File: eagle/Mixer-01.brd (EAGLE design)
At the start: 95 x 72 mm, 58 parts, among them IC1 TL072P, IC2 TL072P, IC3 LM4558N

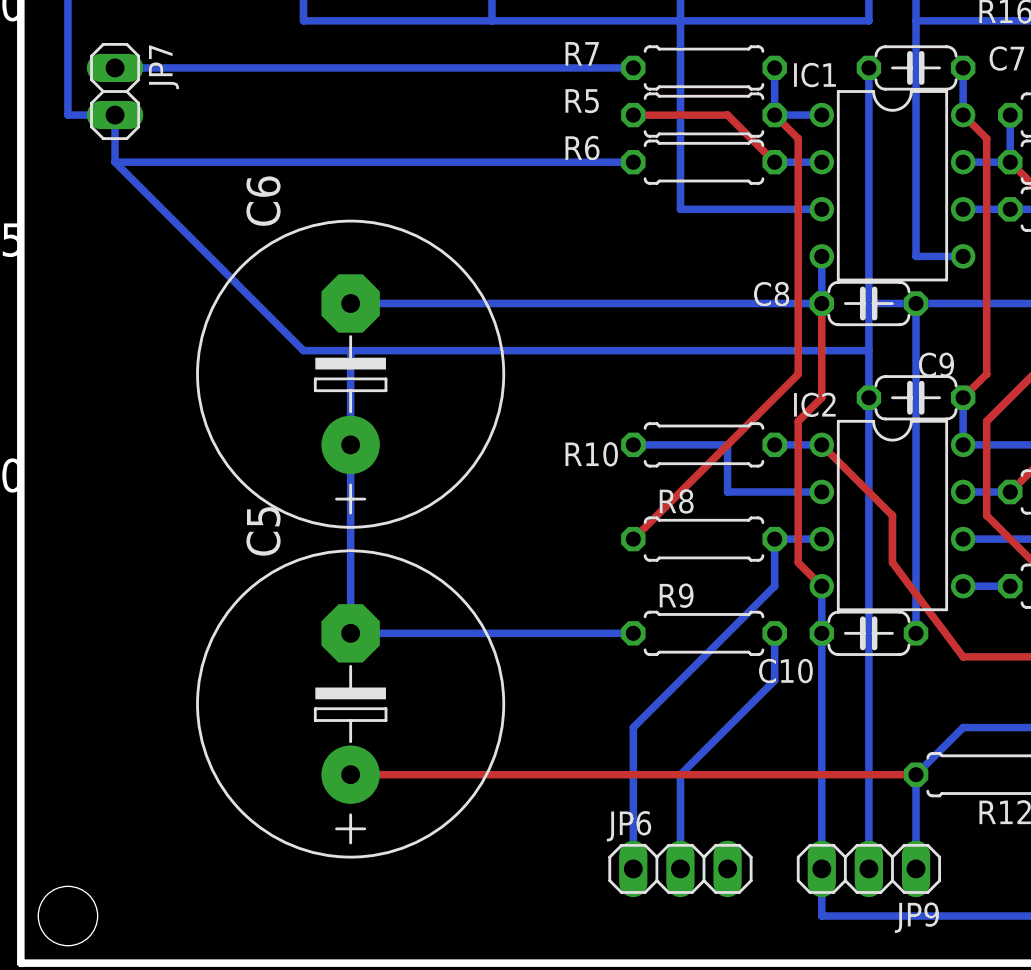
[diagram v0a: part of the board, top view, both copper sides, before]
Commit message: Mixer-01.brd: 修正
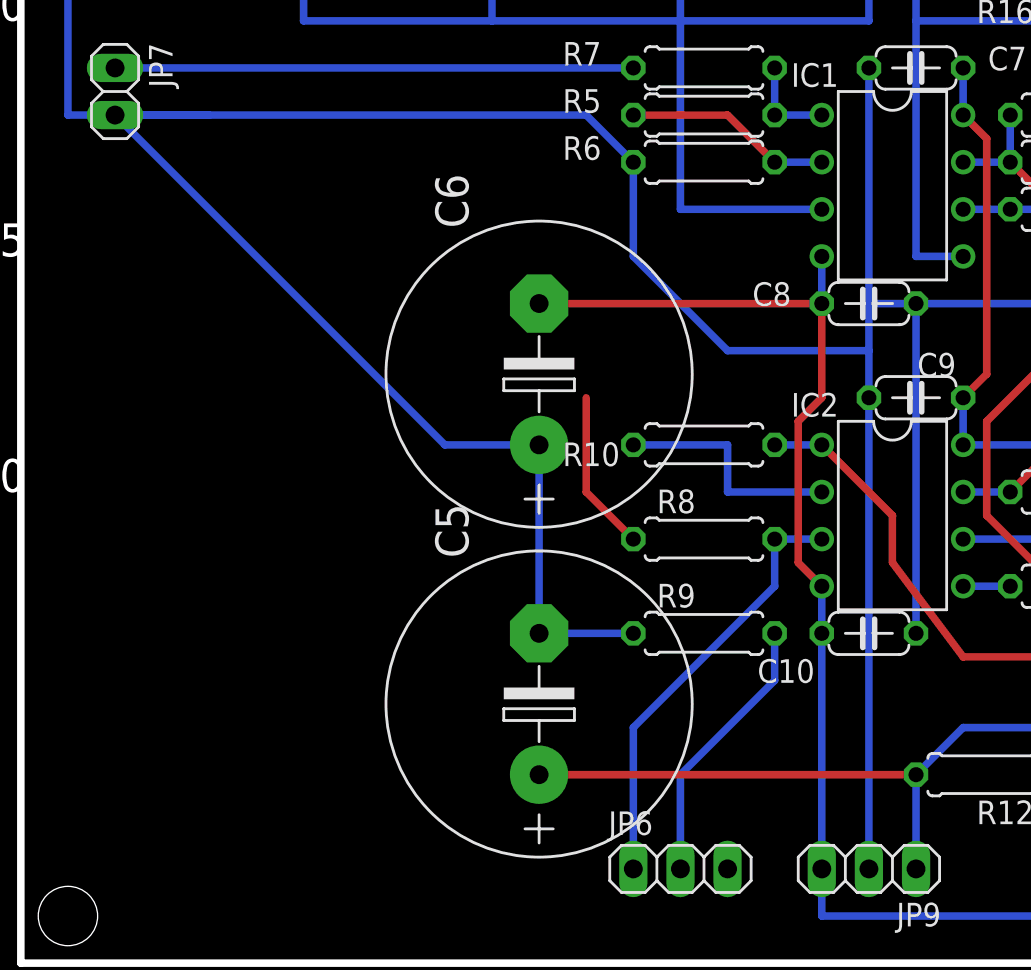
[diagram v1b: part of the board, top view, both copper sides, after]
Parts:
- C5, C6: device resistor:E7,5-16 -> rcl:E7,5-16
- moved C5 10.2 mm to (27.9, 14.0)
- moved C6 10.2 mm to (27.9, 31.8)
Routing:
- net N$15: track 32.1 -> 13.8 mm
- net V-: track 114.9 -> 104.8 mm
- net V+: track 99.2 -> 89.1 mm
- net GND: track 269.4 -> 263.0 mm
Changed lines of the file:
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@@
 <layer number="97" name="Info" color="7" fill="1" visible="no" active="no"/>
 <layer number="98" name="Guide" color="6" fill="1" visible="no" active="no"/>
-<layer number="100" name="Grid" color="7" fill="1" visible="yes" active="yes"/>
+<layer number="100" name="Grid" color="7" fill="1" visible="no" active="yes"/>
 <layer number="101" name="Jumper" color="14" fill="1" visible="yes" active="yes"/>
+<layer number="102" name="outline" color="15" fill="1" visible="yes" active="yes"/>
 </layers>
 <board>
@@
 <wire x1="38.1" y1="5.08" x2="38.1" y2="25.4" width="0.4064" layer="101"/>
 <wire x1="0" y1="12.7" x2="93.98" y2="12.7" width="0.254" layer="100"/>
+<wire x1="27.94" y1="39.37" x2="2.54" y2="39.37" width="0.0254" layer="102"/>
+<wire x1="2.54" y1="39.37" x2="2.54" y2="24.13" width="0.0254" layer="102"/>
+<wire x1="2.54" y1="24.13" x2="27.94" y2="24.13" width="0.0254" layer="102"/>
+<wire x1="27.94" y1="24.13" x2="27.94" y2="39.37" width="0.0254" layer="102"/>
+<wire x1="27.94" y1="21.59" x2="2.54" y2="21.59" width="0.0254" layer="102"/>
+<wire x1="2.54" y1="21.59" x2="2.54" y2="6.35" width="0.0254" layer="102"/>
+<wire x1="2.54" y1="6.35" x2="27.94" y2="6.35" width="0.0254" layer="102"/>
+<wire x1="27.94" y1="6.35" x2="27.94" y2="21.59" width="0.0254" layer="102"/>
+<wire x1="30.48" y1="30.48" x2="40.64" y2="45.72" width="0.4064" layer="101"/>
 </plain>
 <attributes>
@@
 <element name="JP10" library="pinhead" package="1X02" value="LED" x="57.15" y="5.08"/>
 <element name="R12" library="resistor" package="0207/7" value="1k" x="52.07" y="10.16" rot="R180"/>
-<element name="C5" library="resistor" package="E7,5-16" value="470u" x="17.78" y="13.97" rot="R90"/>
-<element name="C6" library="resistor" package="E7,5-16" value="470u" x="17.78" y="31.75" rot="R90"/>
+<element name="C5" library="rcl" package="E7,5-16" value="470u" x="27.94" y="13.97" rot="R90"/>
+<element name="C6" library="rcl" package="E7,5-16" value="470u" x="27.94" y="31.75" rot="R90"/>
 <element name="C7" library="resistor" package="C050-024X044" value="0.1u" x="48.26" y="48.26" smashed="yes" rot="R180">
 <attribute name="NAME" x="54.229" y="49.403" size="1.27" layer="25" ratio="10" rot="R180"/>
@@
 <wire x1="55.88" y1="12.7" x2="50.8" y2="12.7" width="0.4064" layer="16"/>
 <wire x1="50.8" y1="12.7" x2="48.26" y2="10.16" width="0.4064" layer="16"/>
-<wire x1="17.78" y1="10.16" x2="48.26" y2="10.16" width="0.4064" layer="1"/>
+<wire x1="27.94" y1="10.16" x2="48.26" y2="10.16" width="0.4064" layer="1"/>
 <wire x1="50.8" y1="45.72" x2="52.07" y2="44.45" width="0.4064" layer="1"/>
 <wire x1="52.07" y1="44.45" x2="52.07" y2="31.75" width="0.4064" layer="1"/>
 <wire x1="52.07" y1="31.75" x2="50.8" y2="30.48" width="0.4064" layer="1"/>
-<wire x1="68.58" y1="27.94" x2="63.5" y2="27.94" width="0" layer="19" extent="16-16"/>
 <wire x1="48.26" y1="5.08" x2="48.26" y2="10.16" width="0.4064" layer="16"/>
+<wire x1="63.5" y1="27.94" x2="68.58" y2="27.94" width="0" layer="19" extent="16-16"/>
 </signal>
 <signal name="V-">
@@
 <wire x1="58.42" y1="2.54" x2="58.42" y2="5.08" width="0.4064" layer="16"/>
 <wire x1="43.18" y1="35.56" x2="43.18" y2="38.1" width="0.4064" layer="16"/>
-<wire x1="17.78" y1="35.56" x2="43.18" y2="35.56" width="0.4064" layer="16"/>
 <wire x1="81.28" y1="20.32" x2="78.74" y2="20.32" width="0.4064" layer="16"/>
 <wire x1="78.74" y1="20.32" x2="78.74" y2="15.24" width="0.4064" layer="16"/>
@@
 <wire x1="41.91" y1="29.21" x2="41.91" y2="21.59" width="0.4064" layer="1"/>
 <wire x1="41.91" y1="21.59" x2="43.18" y2="20.32" width="0.4064" layer="1"/>
+<wire x1="27.94" y1="35.56" x2="43.18" y2="35.56" width="0.4064" layer="1"/>
 </signal>
 <signal name="GND">
@@
 <contactref element="R21" pad="1"/>
 <wire x1="45.72" y1="48.26" x2="45.72" y2="35.56" width="0.4064" layer="16"/>
-<wire x1="45.72" y1="35.56" x2="45.72" y2="33.02" width="0.4064" layer="16"/>
 <wire x1="48.26" y1="35.56" x2="48.26" y2="17.78" width="0.4064" layer="16"/>
 <wire x1="45.72" y1="5.08" x2="45.72" y2="30.48" width="0.4064" layer="16"/>
@@
 <wire x1="60.96" y1="35.56" x2="48.26" y2="35.56" width="0.4064" layer="16"/>
 <wire x1="60.96" y1="40.64" x2="60.96" y2="35.56" width="0.4064" layer="16"/>
-<wire x1="17.78" y1="17.78" x2="17.78" y2="27.94" width="0.4064" layer="16"/>
-<wire x1="17.78" y1="17.78" x2="33.02" y2="17.78" width="0.4064" layer="16"/>
+<wire x1="27.94" y1="17.78" x2="27.94" y2="27.94" width="0.4064" layer="16"/>
+<wire x1="27.94" y1="17.78" x2="33.02" y2="17.78" width="0.4064" layer="16"/>
 <wire x1="45.72" y1="30.48" x2="45.72" y2="33.02" width="0.4064" layer="16"/>
-<wire x1="45.72" y1="33.02" x2="17.78" y2="33.02" width="0.4064" layer="16"/>
-<wire x1="17.78" y1="33.02" x2="17.78" y2="27.94" width="0.4064" layer="16"/>
-<wire x1="17.78" y1="33.02" x2="15.24" y2="33.02" width="0.4064" layer="16"/>
-<wire x1="5.08" y1="43.18" x2="5.08" y2="45.72" width="0.4064" layer="16"/>
+<wire x1="45.72" y1="33.02" x2="45.72" y2="35.56" width="0.4064" layer="16"/>
 <wire x1="88.9" y1="25.4" x2="91.44" y2="25.4" width="0.4064" layer="16"/>
 <wire x1="91.44" y1="25.4" x2="91.44" y2="43.18" width="0.4064" layer="16"/>
 <wire x1="91.44" y1="43.18" x2="88.9" y2="43.18" width="0.4064" layer="16"/>
-<wire x1="33.02" y1="43.18" x2="5.08" y2="43.18" width="0.4064" layer="16"/>
 <wire x1="48.26" y1="35.56" x2="45.72" y2="35.56" width="0.4064" layer="16"/>
 <wire x1="5.08" y1="53.34" x2="2.54" y2="53.34" width="0.4064" layer="16"/>
 <wire x1="2.54" y1="53.34" x2="2.54" y2="45.72" width="0.4064" layer="16"/>
 <wire x1="2.54" y1="45.72" x2="5.08" y2="45.72" width="0.4064" layer="16"/>
-<wire x1="5.08" y1="43.18" x2="15.24" y2="33.02" width="0.4064" layer="16"/>
+<wire x1="10.16" y1="45.72" x2="5.08" y2="45.72" width="0.4064" layer="16"/>
+<wire x1="33.02" y1="43.18" x2="30.48" y2="45.72" width="0.4064" layer="16"/>
+<wire x1="30.48" y1="45.72" x2="5.08" y2="45.72" width="0.4064" layer="16"/>
+<wire x1="33.02" y1="43.18" x2="33.02" y2="38.1" width="0.4064" layer="16"/>
+<wire x1="33.02" y1="38.1" x2="38.1" y2="33.02" width="0.4064" layer="16"/>
+<wire x1="38.1" y1="33.02" x2="45.72" y2="33.02" width="0.4064" layer="16"/>
+<wire x1="27.94" y1="27.94" x2="22.86" y2="27.94" width="0.4064" layer="16"/>
+<wire x1="22.86" y1="27.94" x2="5.08" y2="45.72" width="0.4064" layer="16"/>
 </signal>
 <signal name="N$9">
@@
 <wire x1="40.64" y1="45.72" x2="43.18" y2="45.72" width="0.4064" layer="16"/>
 <wire x1="40.64" y1="45.72" x2="40.64" y2="48.26" width="0.4064" layer="16"/>
-<wire x1="40.64" y1="45.72" x2="41.91" y2="44.45" width="0.4064" layer="1"/>
-<wire x1="41.91" y1="44.45" x2="41.91" y2="31.75" width="0.4064" layer="1"/>
-<wire x1="41.91" y1="31.75" x2="33.02" y2="22.86" width="0.4064" layer="1"/>
+<wire x1="30.48" y1="30.48" x2="30.48" y2="25.4" width="0.4064" layer="1"/>
+<wire x1="30.48" y1="25.4" x2="33.02" y2="22.86" width="0.4064" layer="1"/>
+<wire x1="30.48" y1="30.48" x2="40.64" y2="45.72" width="0" layer="19" extent="1-1"/>
 </signal>
 <signal name="N$16">
